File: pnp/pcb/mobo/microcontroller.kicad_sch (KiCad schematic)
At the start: 32 parts, among them J1 SWD Header, J32 BOOT_JUMPER, SW1 SW_Push, SW2 SW_Push, U1 STM32F407VETx, Y1 8MHz

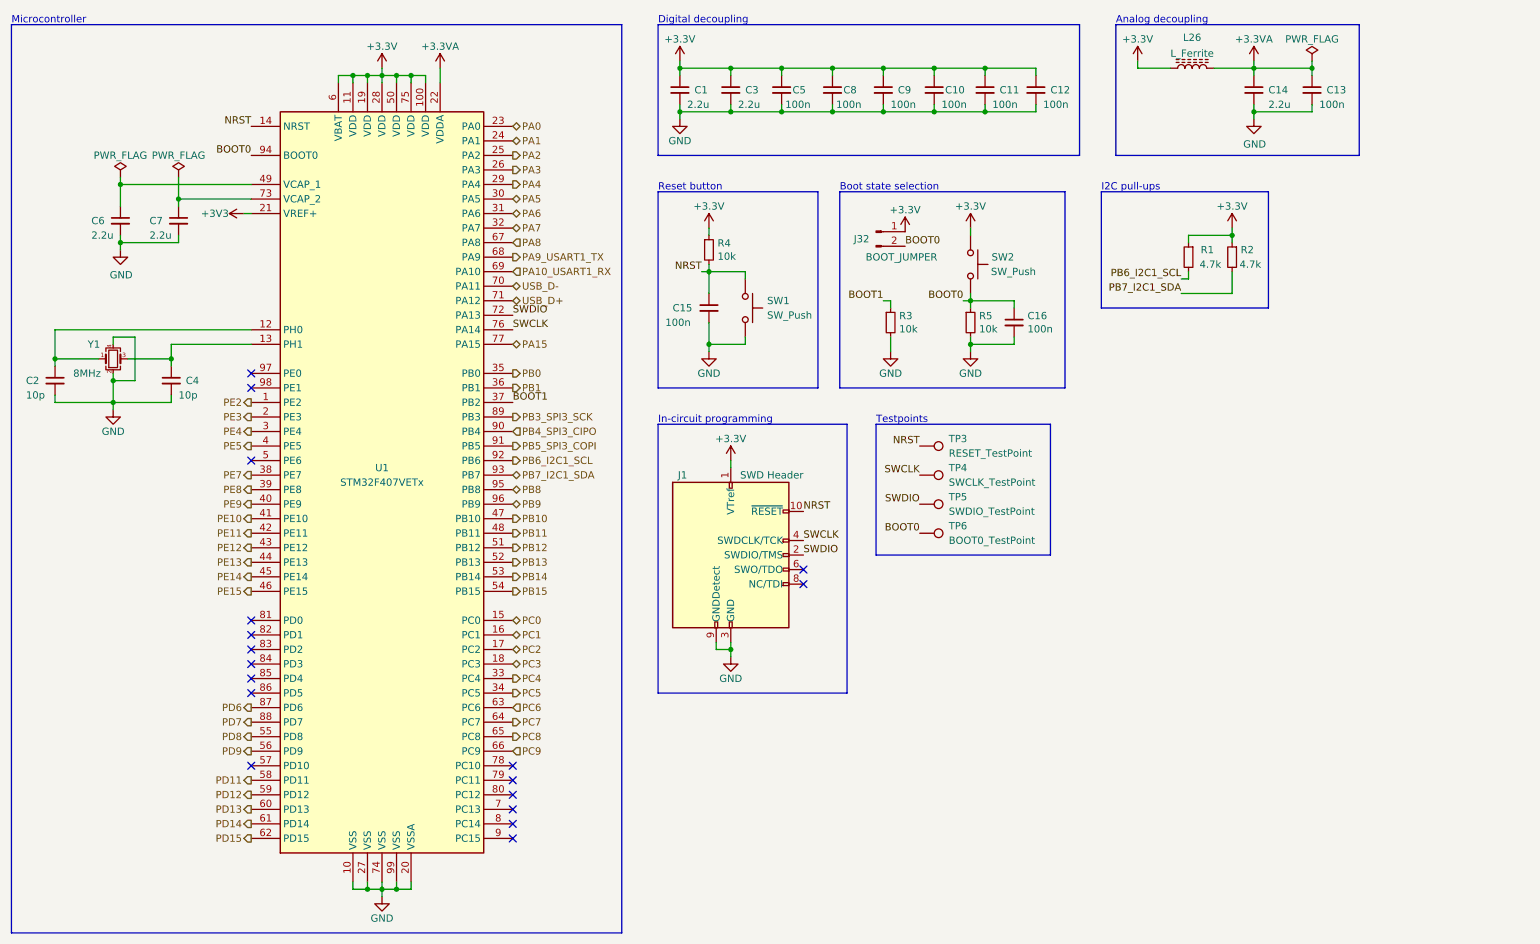
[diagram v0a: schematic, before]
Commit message: Mobo V4A Redesign
Some EMC improvements to schematics.
Reassigned MCU Pins for HW-PWM support.
Changes are still marked with text in the schematics.
Complete PCB Layout reworked
Status: Needs to be verified, and cleaned up a little, but DRC is running green.
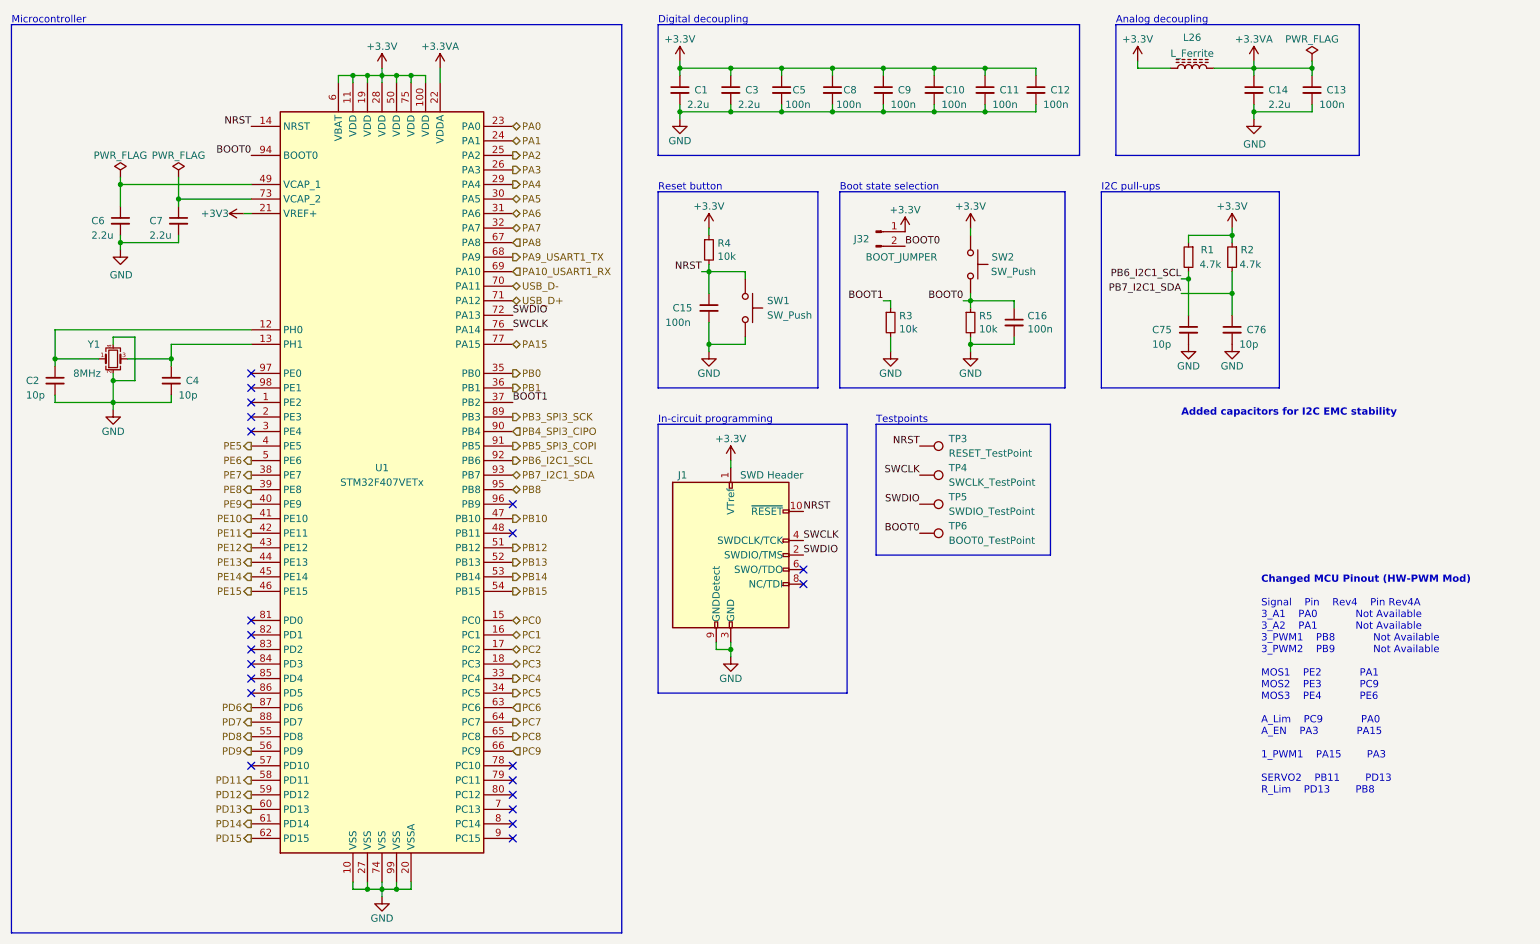
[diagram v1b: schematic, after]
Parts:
- added C75, C76: 10p, Capacitor_SMD:C_0805_2012Metric, symbol Device:C_Small
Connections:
- net GND: now also C75.2, C76.2
- net PB6_I2C1_SCL: now also C75.1
- net PB7_I2C1_SDA: now also C76.1
- net PE6: now reaches U1.5 (PE6)
- net PB11: no longer names the net of U1.48 (PB11)
- net PB9: no longer names the net of U1.96 (PB9)
- net PE2: no longer names the net of U1.1 (PE2)
- net PE3: no longer names the net of U1.2 (PE3)
- net PE4: no longer names the net of U1.3 (PE4)
- no-connect marks 18 -> 22
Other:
- note added: "Added capacitors for I2C EMC stability"
- note added: "Changed MCU Pinout (HW-PWM Mod)"
- note added: "Signal Pin Rev4 Pin Rev4A 3_A1 PA0 Not Available 3_A2 PA1 Not Available 3_PWM1 PB8 Not Available 3_PWM2 PB9 Not Available MOS1 PE2 PA1 MOS2 PE3 PC9 MOS3 PE4 PE6 A_Lim PC9 PA0 A_EN PA3 PA15 1_PWM1 PA15 PA3 SERVO2 PB11 PD13 R_Lim PD13 PB8"
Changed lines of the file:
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@@
   (title_block
     (title "LumenPnP Motherboard")
-    (date "2022-03-29")
+    (date "2022-09-09")
+    (rev "004A")
     (company "Opulo")
+    (comment 1 "Reengineered by Magpie")
   )
   (junction (at 167.64 43.18) (diameter 0) (color 0 0 0 0)
@@
   (junction (at 176.53 35.56) (diameter 0) (color 0 0 0 0)
   )
+  (junction (at 229.87 72.39) (diameter 0) (color 0 0 0 0)
+  )
   (junction (at 86.36 36.83) (diameter 0) (color 0 0 0 0)
   )
@@
   )
   (junction (at 149.86 43.18) (diameter 0) (color 0 0 0 0)
+  )
+  (junction (at 237.49 74.93) (diameter 0) (color 0 0 0 0)
   )
   (junction (at 83.82 36.83) (diameter 0) (color 0 0 0 0)
@@
   (no_connect (at 162.56 123.19))
   (no_connect (at 66.04 157.48))
+  (no_connect (at 111.76 111.76))
+  (no_connect (at 111.76 116.84))
+  (no_connect (at 66.04 99.06))
   (no_connect (at 66.04 134.62))
+  (no_connect (at 66.04 93.98))
   (no_connect (at 66.04 142.24))
   (no_connect (at 66.04 137.16))
   (no_connect (at 66.04 144.78))
-  (no_connect (at 66.04 104.14))
   (no_connect (at 66.04 91.44))
   (no_connect (at 111.76 162.56))
@@
   (no_connect (at 162.56 125.73))
   (no_connect (at 111.76 160.02))
+  (no_connect (at 66.04 96.52))
   (no_connect (at 111.76 167.64))
   (no_connect (at 66.04 139.7))
@@
     (stroke (width 0) (type default) (color 0 0 0 0))
   )
-  (polyline (pts (xy 214.63 57.15) (xy 214.63 77.47))
+  (polyline (pts (xy 214.63 57.15) (xy 214.63 91.44))
     (stroke (width 0) (type default) (color 0 0 0 0))
   )
@@
     (stroke (width 0) (type default) (color 0 0 0 0))
   )
-  (polyline (pts (xy 243.84 57.15) (xy 243.84 77.47))
+  (polyline (pts (xy 245.745 57.15) (xy 245.745 91.44))
     (stroke (width 0) (type default) (color 0 0 0 0))
   )
@@
     (stroke (width 0) (type default) (color 0 0 0 0))
   )
+  (wire (pts (xy 237.49 74.93) (xy 237.49 78.74))
+    (stroke (width 0) (type default) (color 0 0 0 0))
+  )
   (wire (pts (xy 81.28 38.1) (xy 81.28 36.83))
     (stroke (width 0) (type default) (color 0 0 0 0))
@@
     (stroke (width 0) (type default) (color 0 0 0 0))
   )
-  (polyline (pts (xy 214.63 57.15) (xy 243.84 57.15))
+  (polyline (pts (xy 214.63 57.15) (xy 245.745 57.15))
     (stroke (width 0) (type default) (color 0 0 0 0))
   )
@@
     (stroke (width 0) (type default) (color 0 0 0 0))
   )
-  (polyline (pts (xy 243.84 77.47) (xy 214.63 77.47))
+  (polyline (pts (xy 245.745 91.44) (xy 214.63 91.44))
     (stroke (width 0) (type default) (color 0 0 0 0))
   )
@@
   )
   (wire (pts (xy 191.77 83.82) (xy 199.39 83.82))
+    (stroke (width 0) (type default) (color 0 0 0 0))
+  )
+  (wire (pts (xy 229.87 72.39) (xy 229.87 78.74))
     (stroke (width 0) (type default) (color 0 0 0 0))
   )
@@
     (effects (font (size 1.27 1.27)) (justify left bottom))
   )
+  (text "Signal	Pin	Rev4	Pin Rev4A\n3_A1	PA0			Not Available\n3_A2	PA1			Not Available\n3_PWM1	PB8			Not Available\n3_PWM2	PB9			Not Available\n\nMOS1	PE2			PA1\nMOS2	PE3			PC9\nMOS3	PE4			PE6\n\nA_Lim	PC9			PA0\nA_EN	PA3			PA15\n\n1_PWM1	PA15		PA3\n\nSERVO2	PB11		PD13\nR_Lim	PD13		PB8"
+    (at 242.57 162.56 0)
+    (effects (font (size 1.27 1.27)) (justify left bottom))
+  )
   (text "Microcontroller" (at 24.13 27.94 0)
     (effects (font (size 1.27 1.27)) (justify left bottom))
@@
     (effects (font (size 1.27 1.27)) (justify left bottom))
   )
+  (text "Added capacitors for I2C EMC stability" (at 228.6 96.52 0)
+    (effects (font (size 1.27 1.27) (thickness 0.254) bold) (justify left bottom))
+  )
   (text "Testpoints" (at 175.26 97.79 0)
     (effects (font (size 1.27 1.27)) (justify left bottom))
@@
     (effects (font (size 1.27 1.27)) (justify left bottom))
   )
+  (text "Changed MCU Pinout (HW-PWM Mod)" (at 242.57 125.73 0)
+    (effects (font (size 1.27 1.27) (thickness 0.254) bold) (justify left bottom))
+  )
   (text "I2C pull-ups" (at 214.63 57.15 0)
     (effects (font (size 1.27 1.27)) (justify left bottom))
@@
     (effects (font (size 1.27 1.27)) (justify left))
   )
-  (hierarchical_label "PE4" (shape output) (at 66.04 99.06 180)
-    (effects (font (size 1.27 1.27)) (justify right))
-  )
   (hierarchical_label "PE9" (shape output) (at 66.04 111.76 180)
     (effects (font (size 1.27 1.27)) (justify right))
@@
     (effects (font (size 1.27 1.27)) (justify right))
   )
-  (hierarchical_label "PE2" (shape output) (at 66.04 93.98 180)
-    (effects (font (size 1.27 1.27)) (justify right))
-  )
   (hierarchical_label "PA6" (shape bidirectional) (at 111.76 60.96 0)
     (effects (font (size 1.27 1.27)) (justify left))
@@
     (effects (font (size 1.27 1.27)) (justify left))
   )
-  (hierarchical_label "PE3" (shape output) (at 66.04 96.52 180)
-    (effects (font (size 1.27 1.27)) (justify right))
-  )
   (hierarchical_label "PD15" (shape output) (at 66.04 170.18 180)
     (effects (font (size 1.27 1.27)) (justify right))
@@
     (effects (font (size 1.27 1.27)) (justify left))
   )
-  (hierarchical_label "PB9" (shape bidirectional) (at 111.76 111.76 0)
-    (effects (font (size 1.27 1.27)) (justify left))
-  )
   (hierarchical_label "PB6_I2C1_SCL" (shape output) (at 111.76 104.14 0)
     (effects (font (size 1.27 1.27)) (justify left))
@@
     (effects (font (size 1.27 1.27)) (justify right))
   )
-  (hierarchical_label "PB11" (shape output) (at 111.76 116.84 0)
-    (effects (font (size 1.27 1.27)) (justify left))
-  )
   (hierarchical_label "PA10_USART1_RX" (shape input) (at 111.76 71.12 0)
     (effects (font (size 1.27 1.27)) (justify left))
@@
     (effects (font (size 1.27 1.27)) (justify right))
   )
+  (hierarchical_label "PE6" (shape output) (at 66.04 104.14 180)
+    (effects (font (size 1.27 1.27)) (justify right))
+  )
   (hierarchical_label "PD12" (shape output) (at 66.04 162.56 180)
     (effects (font (size 1.27 1.27)) (justify right))
@@
     (pin "1")
     (pin "2")
+  )
+  (symbol (lib_id "power:GND") (at 237.49 83.82 0) (unit 1)
+    (in_bom yes) (on_board yes)
+    (property "Reference" "#PWR035" (id 0) (at 237.49 90.17 0)
+      (effects (font (size 1.27 1.27)) hide)
+    )
+    (property "Value" "GND" (id 1) (at 237.49 87.63 0))
+    (property "Footprint" "" (id 2) (at 237.49 83.82 0)
+      (effects (font (size 1.27 1.27)) hide)
+    )
+    (property "Datasheet" "" (id 3) (at 237.49 83.82 0)
+      (effects (font (size 1.27 1.27)) hide)
+    )
+    (pin "1")
   )
   (symbol (lib_id "Device:C_Small") (at 167.64 39.37 0) (unit 1)
@@
     (pin "2")
   )
+  (symbol (lib_id "Device:C_Small") (at 229.87 81.28 0) (unit 1)
+    (in_bom yes) (on_board yes)
+    (property "Reference" "C75" (id 0) (at 223.52 81.28 0)
+      (effects (font (size 1.27 1.27)) (justify left))
+    )
+    (property "Value" "10p" (id 1) (at 223.52 83.82 0)
+      (effects (font (size 1.27 1.27)) (justify left))
+    )
+    (property "Footprint" "Capacitor_SMD:C_0805_2012Metric" (id 2) (at 229.87 81.28 0)
+      (effects (font (size 1.27 1.27)) hide)
+    )
+    (property "Datasheet" "" (id 3) (at 229.87 81.28 0)
+      (effects (font (size 1.27 1.27)) hide)
+    )
+    (property "Digikey" "" (id 4) (at 229.87 81.28 0)
+      (effects (font (size 1.27 1.27)) hide)
+    )
+    (property "JLCPCB" "C1785" (id 5) (at 229.87 81.28 0)
+      (effects (font (size 1.27 1.27)) hide)
+    )
+    (property "LCSC" "C525280" (id 6) (at 229.87 81.28 0)
+      (effects (font (size 1.27 1.27)) hide)
+    )
+    (property "Mouser" "" (id 7) (at 229.87 81.28 0)
+      (effects (font (size 1.27 1.27)) hide)
+    )
+    (pin "1")
+    (pin "2")
+  )
   (symbol (lib_id "Device:R_Small") (at 177.8 80.01 0) (unit 1)
     (in_bom yes) (on_board yes)
@@
     )
     (pin "1")
+  )
+  (symbol (lib_id "Device:C_Small") (at 237.49 81.28 0) (unit 1)
+    (in_bom yes) (on_board yes)
+    (property "Reference" "C76" (id 0) (at 240.03 81.28 0)
+      (effects (font (size 1.27 1.27)) (justify left))
+    )
+    (property "Value" "10p" (id 1) (at 238.76 83.82 0)
+      (effects (font (size 1.27 1.27)) (justify left))
+    )
+    (property "Footprint" "Capacitor_SMD:C_0805_2012Metric" (id 2) (at 237.49 81.28 0)
+      (effects (font (size 1.27 1.27)) hide)
+    )
+    (property "Datasheet" "" (id 3) (at 237.49 81.28 0)
+      (effects (font (size 1.27 1.27)) hide)
+    )
+    (property "Digikey" "" (id 4) (at 237.49 81.28 0)
+      (effects (font (size 1.27 1.27)) hide)
+    )
+    (property "JLCPCB" "C1785" (id 5) (at 237.49 81.28 0)
+      (effects (font (size 1.27 1.27)) hide)
+    )
+    (property "LCSC" "C525280" (id 6) (at 237.49 81.28 0)
+      (effects (font (size 1.27 1.27)) hide)
+    )
+    (property "Mouser" "" (id 7) (at 237.49 81.28 0)
+      (effects (font (size 1.27 1.27)) hide)
+    )
+    (pin "1")
+    (pin "2")
   )
   (symbol (lib_id "power:GND") (at 177.8 85.09 0) (unit 1)
@@
       (effects (font (size 1.27 1.27)) hide)
     )
+    (pin "1")
+  )
+  (symbol (lib_id "power:GND") (at 229.87 83.82 0) (unit 1)
+    (in_bom yes) (on_board yes)
+    (property "Reference" "#PWR034" (id 0) (at 229.87 90.17 0)
+      (effects (font (size 1.27 1.27)) hide)
+    )
+    (property "Value" "GND" (id 1) (at 229.87 87.63 0))
+    (property "Footprint" "" (id 2) (at 229.87 83.82 0)
+      (effects (font (size 1.27 1.27)) hide)
+    )
+    (property "Datasheet" "" (id 3) (at 229.87 83.82 0)
+      (effects (font (size 1.27 1.27)) hide)
+    )
